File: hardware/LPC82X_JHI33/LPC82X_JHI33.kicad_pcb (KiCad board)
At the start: 2 copper layers, 23.6 x 23.5 mm, 24 parts, among them J1 LPC82XJHI33_LEFT, J2 LPC82XJHI33_RIGHT, J3 JTAG_2X05, U1 LPC824M201JHI33, Y1 12MHz

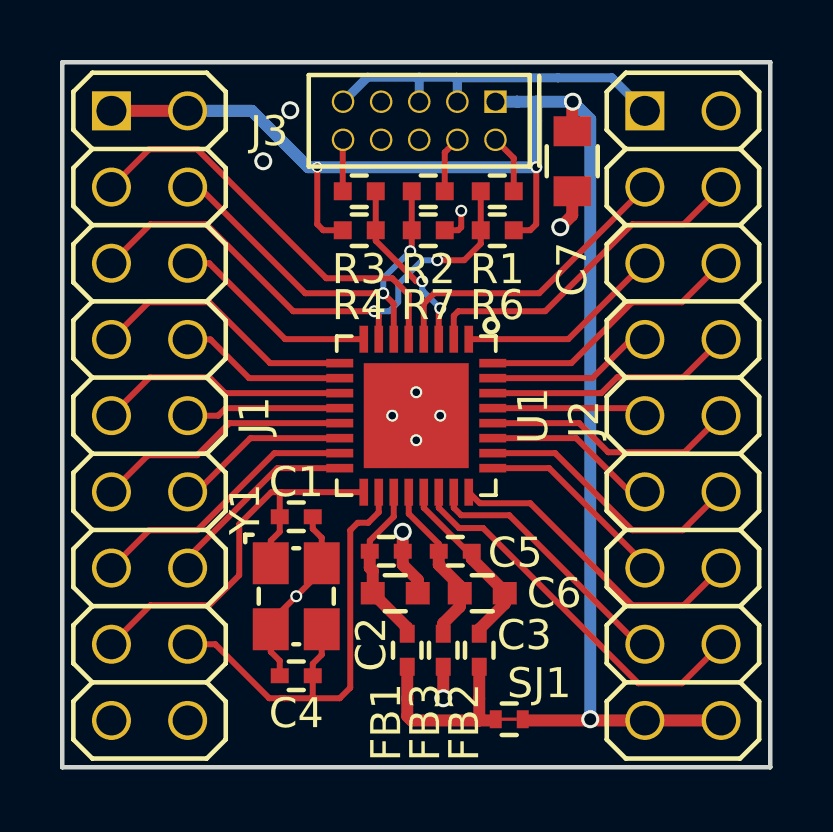
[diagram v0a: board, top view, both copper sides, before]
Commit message: needed relayout as moving stuff off sheet will reset it
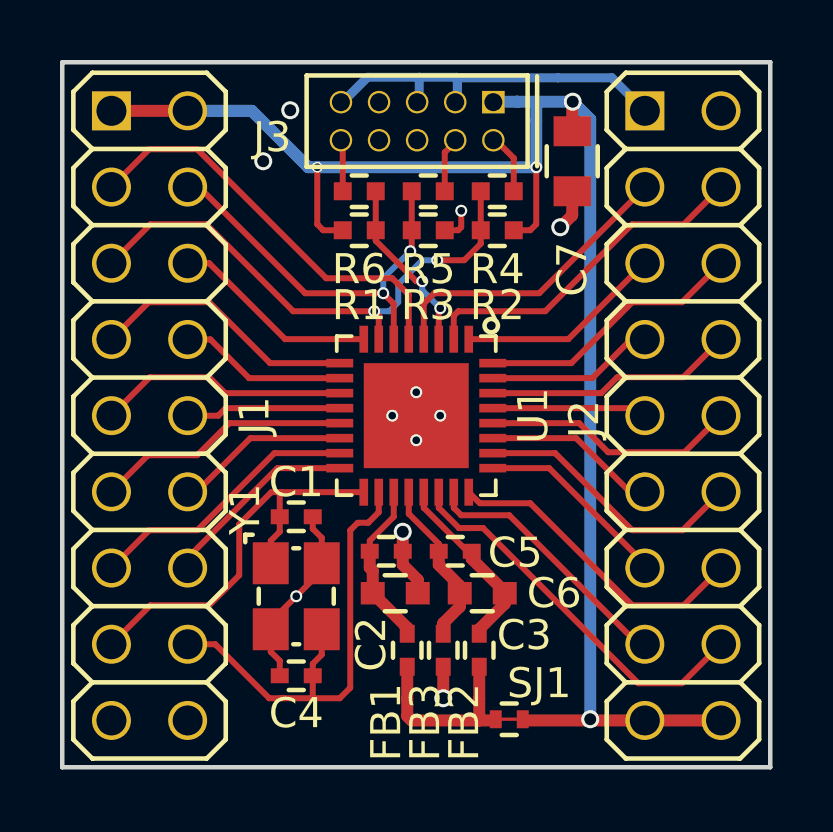
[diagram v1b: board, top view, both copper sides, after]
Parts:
- removed R7: 100k, SquantorRcl:R_0402_hand
- added R5: 100, SquantorRcl:R_0402_hand, F.Cu at (89.3, 99.2)
- N2: value 20190514 -> 20190710
- R1: value 100 -> 100K
- R2, R3: value 100 -> 100k
- R4: value 100K -> 100
- R6: value 100k -> 100
- moved R1 4.78 mm to (87.0, 100.5), turned to 0 degrees
- moved R4 4.78 mm to (91.6, 99.2), turned to 180 degrees
- moved R6 4.78 mm to (87.0, 99.2), turned to 0 degrees
- moved R2 2.64 mm to (91.6, 100.5)
- moved R3 2.64 mm to (89.3, 100.5), turned to 180 degrees
- moved J3 0.07 mm to (88.9, 96.9)
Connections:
- R1 pad 1: Net-(J3-Pad2) -> /VDD
- R1 pad 2: /PIO0_2 -> /RESET
- R2 pad 1: Net-(J3-Pad4) -> /VDD
- R2 pad 2: /PIO0_3 -> /PIO0_2
- R3 pad 1: Net-(J3-Pad10) -> /VSS
- R3 pad 2: /RESET -> /PIO0_3
- R4 pad 1: /VDD -> Net-(J3-Pad2)
- R4 pad 2: /RESET -> /PIO0_2
- R6 pad 1: /VDD -> Net-(J3-Pad10)
- R6 pad 2: /PIO0_2 -> /RESET
